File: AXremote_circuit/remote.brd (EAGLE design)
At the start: 60 x 49 mm, 27 parts, among them Q1 16MHz, U1 AX8052F143HS

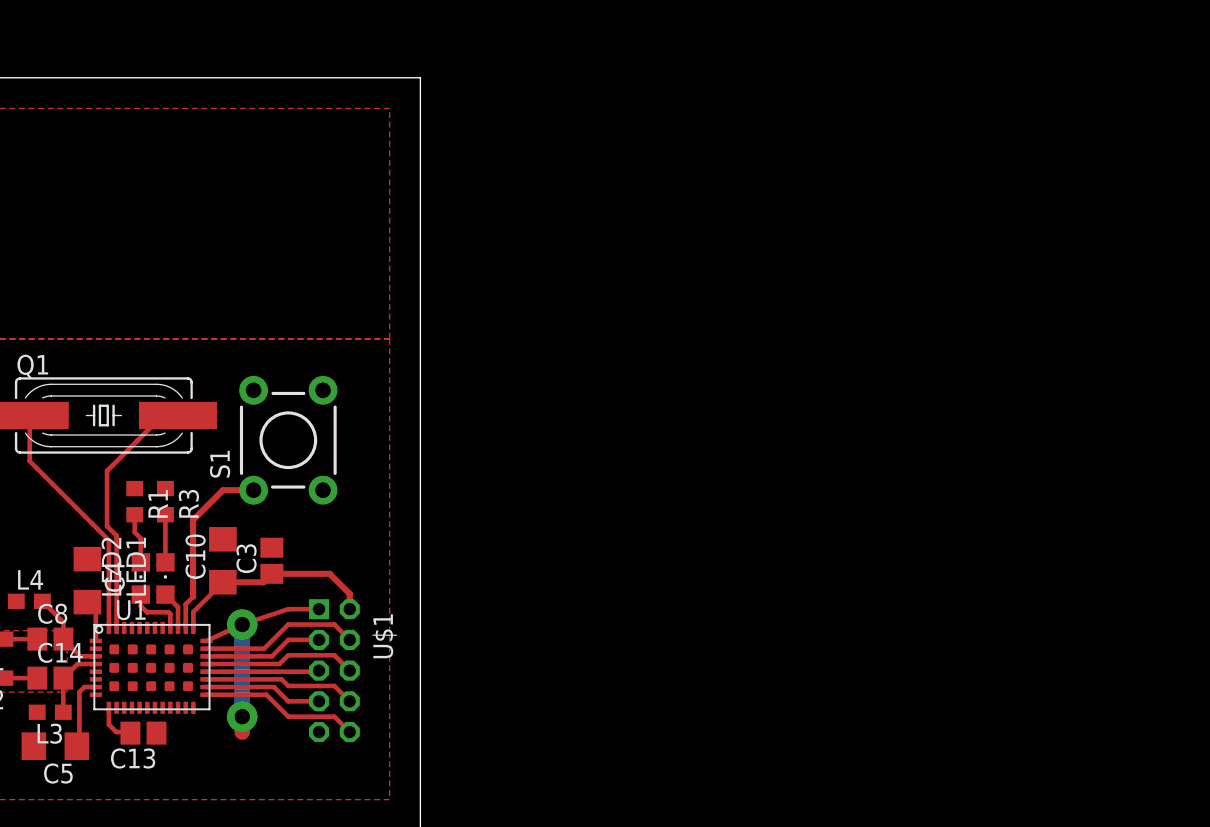
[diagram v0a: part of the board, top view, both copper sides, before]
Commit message: Fix progconnector in schematic. Add TODOs.
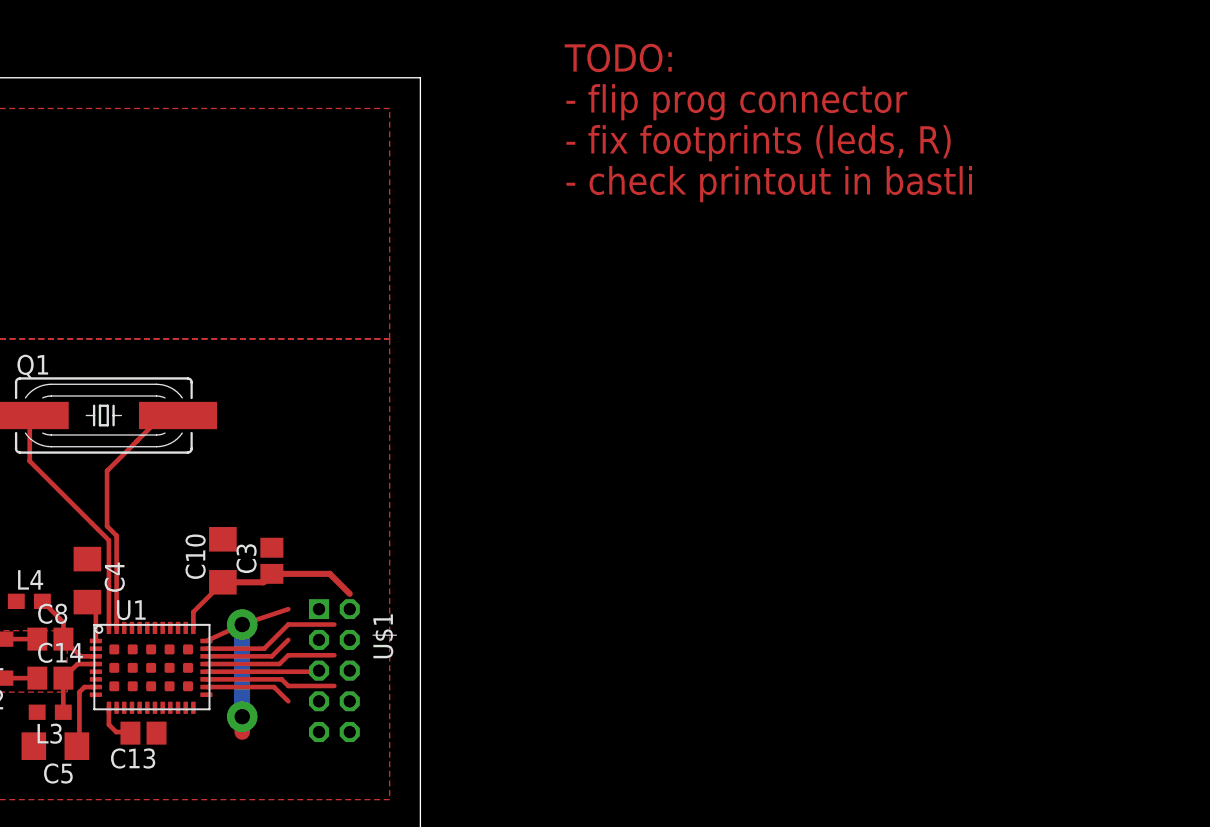
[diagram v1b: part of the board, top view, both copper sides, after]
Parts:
- removed LED1, LED2: (no value), led:CHIPLED_0805
- removed R1, R3: 220, resistor:R0603
- removed S1: SWITCH-MOMENTARY-2PTH, SparkFun-Electromechanical:TACTILE-PTH
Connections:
- removed net N$11: LED1.A, U1.31
- removed net N$18: U$1.P$10, U1.21
- removed net N$19: S1.1, U1.30
- removed net N$4: LED2.C, R1.2
- removed net RST_N: U$1.P$4, U1.27
- new net BATTMEASURE: U1.30
- net DBG_CLK: now also U$1.P$5; no longer U$1.P$6
- net DBG_DATA: now also U$1.P$6; no longer U$1.P$5
- net DBG_EN: now also U$1.P$4; no longer U$1.P$3
- net GND: now also U$1.P$10, U$1.P$2; no longer R1.1, R3.1, S1.3, U$1.P$1, U$1.P$9
- net N$16: now also U$1.P$9, U1.21; no longer LED2.A, U1.32
- net N$5: now also U$1.P$3, U1.27; no longer LED1.C, R3.2
- net RX0: now also U$1.P$7; no longer U$1.P$8
- net TX0: now also U$1.P$8; no longer U$1.P$7
- net VCC: now also U$1.P$1, U1.36; no longer U$1.P$2
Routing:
- net N$19: track 12.0 -> 0.00 mm
- net RST_N: track 10.4 -> 0.00 mm
- net N$18: track 10.3 -> 0.00 mm
- net N$5: track 3.10 -> 8.98 mm
- net N$16: track 3.79 -> 0.00 mm
- net N$4: track 3.27 -> 0.00 mm
- net N$11: track 2.51 -> 0.00 mm
- net TX0: track 7.72 -> 5.72 mm
- net GND: track 41.5 -> 39.5 mm
- net DBG_EN: track 7.77 -> 5.77 mm
- net RX0: track 9.92 -> 8.51 mm
- net DBG_CLK: track 9.98 -> 8.57 mm
- net VCC: track 13.8 -> 12.8 mm
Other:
- board text added: "TODO: - flip prog connector - fix footprints (leds, R) - check printout in bastli"

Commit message: remote almost complete
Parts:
- added C1: 100uF, resistor:PANASONIC_E
- added C2: 100uF, resistor:C1206K
- added JP1: (no value), pinhead:1X02
- added LED1, LED2: (no value), led:CHIPLED_1206
- added R1, R3: (no value), resistor:R0603
- added S1, S10, S11, S12, S13, S14, S15, S16, S17, S18, S19, S2, S20, S21, S22, S23, S24, S25, S28, S3, S30, S4, S41, S42, S43, S44, S45, S46, S5, S6, S7, S8, S9: (no value), switch-omron:B3F-10XX
- added U$2: 2X5PIN-CONNECTOR, sam_eagle_parts:2X5PIN-CONNECTOR-SMD
- C10, C4, C5: device resistor:C1206 -> resistor:C0603
- U$1: value PINHEADER5X2 -> CR2032; device sam:PINHEADER5X2AT2MM -> sam_eagle_parts:CRC2032HOLDER
- moved Q1 39.8 mm to (33.4, 23.0)
- moved U$1 39.5 mm to (58.0, 4.00), turned to 90 degrees
- moved C13 36.4 mm to (39.9, 4.43), turned to 90 degrees
- moved C10 35.8 mm to (46.5, 15.9), turned to 0 degrees
- moved C3 34.2 mm to (46.5, 18.7), turned to 0 degrees
- moved C16 34.0 mm to (30.8, 6.10)
- moved C6 34.0 mm to (23.2, 14.5)
- moved C7 34.0 mm to (23.2, 7.87)
- moved L3 34.0 mm to (35.9, 7.69)
- moved L6 34.0 mm to (28.3, 6.10)
- moved R2 34.0 mm to (24.2, 11.2)
- moved U1 34.0 mm to (42.5, 10.6)
- moved C14 34.0 mm to (35.9, 9.91)
- moved C15 34.0 mm to (28.3, 9.91)
- moved C17 34.0 mm to (29.6, 16.3)
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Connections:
- removed net BATTMEASURE: U1.30
- removed net RX0: U$1.P$7, U1.23
- removed net TX0: U$1.P$8, U1.22
- new net COL0: S1.1, S1.2, S11.1, S11.2, S16.1, S16.2, S21.1, S21.2, S6.1, S6.2, U1.23
- new net COL1: S12.1, S12.2, S17.1, S17.2, S2.1, S2.2, S22.1, S22.2, S7.1, S7.2, U1.22
- new net COL2: S13.1, S13.2, S18.1, S18.2, S23.1, S23.2, S28.1, S28.2, S3.1, S3.2, S8.1, S8.2, U1.21
- new net COL3: S14.1, S14.2, S19.1, S19.2, S24.1, S24.2, S4.1, S4.2, S9.1, S9.2, U1.20
- new net COL4: S10.1, S10.2, S15.1, S15.2, S20.1, S20.2, S25.1, S25.2, S30.1, S30.2, S5.1, S5.2, U1.19
- new net COL5: S41.1, S41.2, S42.1, S42.2, S43.1, S43.2, S44.1, S44.2, S45.1, S45.2, S46.1, S46.2, U1.18
- new net N$11: LED2.A, U1.35
- new net N$17: LED1.C, R1.2
- new net N$4: LED1.A, U1.34
- new net N$64: C1.+, C2.1, JP1.1, U$1.P$PLUS1, U$1.P$PLUS2
- new net ROW0: S1.3, S1.4, S2.3, S2.4, S3.3, S3.4, S4.3, S4.4, S41.3, S41.4, S5.3, S5.4, U1.17
- new net ROW1: S10.3, S10.4, S42.3, S42.4, S6.3, S6.4, S7.3, S7.4, S8.3, S8.4, S9.3, S9.4, U1.16
- new net ROW2: S11.3, S11.4, S12.3, S12.4, S13.3, S13.4, S14.3, S14.4, S15.3, S15.4, S43.3, S43.4, U1.15
- new net ROW3: S16.3, S16.4, S17.3, S17.4, S18.3, S18.4, S19.3, S19.4, S20.3, S20.4, S44.3, S44.4, U1.14
- new net ROW4: S21.3, S21.4, S22.3, S22.4, S23.3, S23.4, S24.3, S24.4, S25.3, S25.4, S45.3, S45.4, U1.13
- new net ROW5: S28.3, S28.4, S30.3, S30.4, S46.3, S46.4, U1.30
- new net ROW6: U1.31
- new net ROW7: U1.32
- new net ROW8: U1.33
- net DBG_CLK: now also U$2.P$5; no longer U$1.P$5
- net DBG_DATA: now also U$2.P$6; no longer U$1.P$6
- net DBG_EN: now also U$2.P$4; no longer U$1.P$4
- net GND: now also C1.-, C2.2, R1.1, R3.1, U$1.P$MINUS, U$2.P$10, U$2.P$2; no longer U$1.P$10, U$1.P$2
- net N$16: now also LED2.C, R3.2; no longer U$1.P$9, U1.21
- net N$5: now also U$2.P$3; no longer U$1.P$3
- net VCC: now also JP1.2, U$2.P$1; no longer U$1.P$1
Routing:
- net COL4: track 0.00 -> 444.3 mm
- net COL2: track 0.00 -> 405.8 mm
- net ROW5: track 0.00 -> 299.6 mm
- net ROW4: track 0.00 -> 283.1 mm
- net ROW0: track 0.00 -> 259.0 mm
- net ROW3: track 0.00 -> 254.0 mm
- net ROW2: track 0.00 -> 237.1 mm
- net COL5: track 0.00 -> 235.7 mm
- net COL0: track 0.00 -> 228.9 mm
- net COL3: track 0.00 -> 221.8 mm
- net COL1: track 0.00 -> 221.0 mm
- net ROW1: track 0.00 -> 176.6 mm
- net VCC: track 12.8 -> 49.0 mm, vias 0 -> 2
- net DBG_EN: track 5.77 -> 38.2 mm
- net DBG_DATA: track 7.26 -> 35.4 mm
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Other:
- board size 60 x 49 mm -> 247.5 x 49 mm
- board text removed: "TODO: - flip prog connector - fix footprints (leds, R) - check printout in bastli"

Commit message: Remote and receiver done.
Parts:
- added U$3: APERTURE_LOGO, sam_eagle_parts:APERTURE_LOGO
- moved Q1 2.00 mm to (31.4, 23.0)
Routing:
- net GND: track 43.3 -> 137.9 mm, vias 2 -> 6
- net N$64: track 25.7 -> 36.2 mm, vias 1 -> 2
- net N$15: track 18.2 -> 20.2 mm
- net COL2: track 405.8 -> 407.2 mm
- net ROW5: track 299.6 -> 301.0 mm
- net COL4: track 444.3 -> 445.3 mm
- net COL3: track 221.8 -> 222.6 mm
- net N$14: track 10.7 -> 11.4 mm
- net ROW0: track 259.0 -> 259.6 mm
- net VCC: track 49.0 -> 49.6 mm
- net COL5: track 235.7 -> 236.3 mm
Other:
- board size 247.5 x 49 mm -> 240 x 49 mm
- board text added: "Samuel Bryner, 2013, rev 2"
- board text removed: "Samuel Bryner, 2013 AX8052F143 Test rev 1b"

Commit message: Added a few keys.
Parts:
- added R4: (no value), resistor:R0603
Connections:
- removed net N$64: C1.+, C2.1, JP1.1, U$1.P$PLUS1, U$1.P$PLUS2
- new net N$18: C1.+, C2.1, JP1.1, R4.2, U$1.P$PLUS1, U$1.P$PLUS2
- net N$5: now also R4.1
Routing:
- net N$18: track 0.00 -> 37.7 mm, vias 0 -> 2
- net N$64: track 36.2 -> 0.00 mm, vias 2 -> 0
- net COL0: track 228.9 -> 235.4 mm
- net GND: track 137.9 -> 139.6 mm
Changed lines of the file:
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@@
 <hole x="87" y="19" drill="3"/>
 <hole x="197" y="45" drill="3"/>
+<hole x="127.5" y="7" drill="3"/>
 </plain>
 <attributes>
@@
 </element>
 <element name="U$3" library="sam_eagle_parts" package="APERTURE_LOGO" value="APERTURE_LOGO" x="178" y="19"/>
+<element name="R4" library="resistor" package="R0603" value="" x="53" y="19" rot="R90"/>
 </elements>
 <signals>
@@
 <wire x1="34" y1="18" x2="33.11" y2="17.11" width="0.4064" layer="1"/>
 <wire x1="33.11" y1="17.11" x2="29.56" y2="17.11" width="0.4064" layer="1"/>
-<wire x1="38.87" y1="9.83" x2="38.87" y2="8.83" width="0" layer="19" extent="1-1"/>
+<wire x1="38.87" y1="9.83" x2="40.07" y2="9.83" width="0.3" layer="1"/>
+<wire x1="40.07" y1="9.83" x2="40.07" y2="9.38" width="0.3" layer="1"/>
 </signal>
 <signal name="N$1">
@@
 <wire x1="53" y1="18" x2="58" y2="18" width="0.3048" layer="1"/>
 <wire x1="58" y1="18" x2="61" y2="21" width="0.3048" layer="1"/>
+<contactref element="R4" pad="1"/>
+<wire x1="53" y1="18.15" x2="53" y2="18" width="0.4064" layer="1"/>
 </signal>
 <signal name="ROW0">
@@
 <wire x1="85.5" y1="41" x2="73" y2="41" width="0.4064" layer="1"/>
 <wire x1="73" y1="41" x2="70" y2="38" width="0.4064" layer="1"/>
-<wire x1="184.4988" y1="39.2606" x2="191.0012" y2="39.2606" width="0" layer="19" extent="1-1"/>
+<wire x1="184.4988" y1="39.2606" x2="191.0012" y2="39.2606" width="0.4064" layer="16"/>
 </signal>
 <signal name="ROW1">
@@
 <signal name="ROW7">
 <contactref element="U1" pad="32"/>
-</signal>
-<signal name="N$64">
-<contactref element="C2" pad="1"/>
-<contactref element="C1" pad="+"/>
-<contactref element="JP1" pad="1"/>
-<contactref element="U$1" pad="P$PLUS2"/>
-<contactref element="U$1" pad="P$PLUS1"/>
-<wire x1="56" y1="21" x2="52.5" y2="21" width="0.4064" layer="1"/>
-<wire x1="52.5" y1="21" x2="51" y2="22.5" width="0.4064" layer="1"/>
-<via x="51" y="19" extent="1-16" drill="0.9" diameter="1.4224" shape="square"/>
-<wire x1="51" y1="19" x2="51" y2="22.5" width="0.4064" layer="1"/>
-<wire x1="58.5" y1="29.73" x2="58.5" y2="23.5" width="0.4064" layer="1"/>
-<wire x1="58.5" y1="23.5" x2="56" y2="21" width="0.4064" layer="1"/>
-<wire x1="52.92" y1="9.08" x2="52.92" y2="10.479771875" width="0.4064" layer="1"/>
-<wire x1="52.92" y1="10.479771875" x2="52.92" y2="11.62" width="0.4064" layer="1"/>
-<wire x1="52.92" y1="10.479771875" x2="50.979771875" y2="10.479771875" width="0.4064" layer="1"/>
-<wire x1="50.979771875" y1="10.479771875" x2="50.5" y2="10" width="0.4064" layer="1"/>
-<via x="50.5" y="10" extent="1-16" drill="0.9" diameter="1.4224" shape="square"/>
-<wire x1="50.5" y1="10" x2="50.5" y2="18.5" width="0.4064" layer="16"/>
-<wire x1="50.5" y1="18.5" x2="51" y2="19" width="0.4064" layer="16"/>
-<wire x1="50.5" y1="10" x2="51.5" y2="9" width="0.4064" layer="1"/>
-<wire x1="51.5" y1="9" x2="53" y2="9" width="0.4064" layer="1"/>
 </signal>
 <signal name="COL1">
@@
 <wire x1="56" y1="39" x2="56" y2="41" width="0.4064" layer="1"/>
 <wire x1="56" y1="41" x2="58" y2="43" width="0.4064" layer="1"/>
-<wire x1="147" y1="43" x2="192.5" y2="43" width="0.4064" layer="1"/>
-<wire x1="192.5" y1="43" x2="194.5" y2="41" width="0.4064" layer="1"/>
-<wire x1="194.5" y1="41" x2="199.5" y2="41" width="0.4064" layer="1"/>
-<wire x1="199.5" y1="41" x2="201.5" y2="43" width="0.4064" layer="1"/>
-<wire x1="201.5" y1="43" x2="211.5" y2="43" width="0.4064" layer="1"/>
+<wire x1="147" y1="43" x2="192" y2="43" width="0.4064" layer="1"/>
+<wire x1="192" y1="43" x2="194" y2="41" width="0.4064" layer="1"/>
+<wire x1="194" y1="41" x2="200" y2="41" width="0.4064" layer="1"/>
+<wire x1="200" y1="41" x2="202" y2="43" width="0.4064" layer="1"/>
+<wire x1="202" y1="43" x2="211.5" y2="43" width="0.4064" layer="1"/>
 </signal>
 <signal name="COL3">
@@
 <wire x1="136" y1="14" x2="122.5118" y2="14" width="0.4064" layer="1"/>
 <wire x1="122.5118" y1="14" x2="122.2512" y2="14.2606" width="0.4064" layer="1"/>
-<wire x1="212" y1="44" x2="201" y2="44" width="0.4064" layer="1"/>
-<wire x1="201" y1="44" x2="199" y2="42" width="0.4064" layer="1"/>
-<wire x1="199" y1="42" x2="195" y2="42" width="0.4064" layer="1"/>
-<wire x1="195" y1="42" x2="193" y2="44" width="0.4064" layer="1"/>
-<wire x1="193" y1="44" x2="147.5" y2="44" width="0.4064" layer="1"/>
+<wire x1="212" y1="44" x2="201.5" y2="44" width="0.4064" layer="1"/>
+<wire x1="201.5" y1="44" x2="199.5" y2="42" width="0.4064" layer="1"/>
+<wire x1="199.5" y1="42" x2="194.5" y2="42" width="0.4064" layer="1"/>
+<wire x1="194.5" y1="42" x2="192.5" y2="44" width="0.4064" layer="1"/>
+<wire x1="192.5" y1="44" x2="147.5" y2="44" width="0.4064" layer="1"/>
 </signal>
 <signal name="N$4">
@@
 <contactref element="R3" pad="2"/>
 <contactref element="LED2" pad="C"/>
-<wire x1="29.75" y1="30" x2="28" y2="30" width="0.3048" layer="1"/>
-<wire x1="27.85" y1="30" x2="28" y2="30" width="0" layer="19" extent="1-1"/>
+<wire x1="27.85" y1="30" x2="29.75" y2="30" width="0.4064" layer="1"/>
 </signal>
 <signal name="N$17">
@@
 <wire x1="134.4988" y1="12.2606" x2="134.4988" y2="11.5012" width="0.4064" layer="1"/>
 </signal>
+<signal name="N$18">
+<contactref element="R4" pad="2"/>
+<contactref element="C2" pad="1"/>
+<contactref element="C1" pad="+"/>
+<contactref element="JP1" pad="1"/>
+<contactref element="U$1" pad="P$PLUS2"/>
+<contactref element="U$1" pad="P$PLUS1"/>
+<wire x1="56" y1="21" x2="53" y2="21" width="0.4064" layer="1"/>
+<wire x1="53" y1="21" x2="52.5" y2="21" width="0.4064" layer="1"/>
+<wire x1="52.5" y1="21" x2="51" y2="22.5" width="0.4064" layer="1"/>
+<via x="50" y="18" extent="1-16" drill="0.9" diameter="1.4224" shape="square"/>
+<wire x1="58.5" y1="29.73" x2="58.5" y2="23.5" width="0.4064" layer="1"/>
+<wire x1="58.5" y1="23.5" x2="56" y2="21" width="0.4064" layer="1"/>
+<wire x1="52.92" y1="9.08" x2="52.92" y2="10.479771875" width="0.4064" layer="1"/>
+<wire x1="52.92" y1="10.479771875" x2="52.92" y2="11.62" width="0.4064" layer="1"/>
+<wire x1="52.92" y1="10.479771875" x2="50.979771875" y2="10.479771875" width="0.4064" layer="1"/>
+<wire x1="50.979771875" y1="10.479771875" x2="50.5" y2="10" width="0.4064" layer="1"/>
+<via x="50.5" y="10" extent="1-16" drill="0.9" diameter="1.4224" shape="square"/>
+<wire x1="50.5" y1="10" x2="50.5" y2="17.5" width="0.4064" layer="16"/>
+<wire x1="50.5" y1="17.5" x2="50" y2="18" width="0.4064" layer="16"/>
+<wire x1="50.5" y1="10" x2="51.5" y2="9" width="0.4064" layer="1"/>
+<wire x1="51.5" y1="9" x2="53" y2="9" width="0.4064" layer="1"/>
+<wire x1="53" y1="19.85" x2="53" y2="21" width="0.4064" layer="1"/>
+<wire x1="51" y1="22.5" x2="51" y2="19" width="0.4064" layer="1"/>
+<wire x1="51" y1="19" x2="50" y2="18" width="0.4064" layer="1"/>
+</signal>
 </signals>

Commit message: Start rev 3, full SMD.
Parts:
- removed JP1: (no value), pinhead:1X02
- removed S41, S42, S43, S44, S45, S46: (no value), switch-omron:B3F-10XX
- added S26, S27, S29, S31, S32, S34: SWITCHSMD, sam:TACTILE_SWITCH_FSM2JSMA
- S1, S10, S11, S12, S13, S14, S15, S16, S17, S18, S19, S2, S20, S21, S22, S23, S24, S25, S28, S3, S30, S4, S5, S6, S7, S8, S9: value (none) -> SWITCHSMD; device switch-omron:B3F-10XX -> sam:TACTILE_SWITCH_FSM2JSMA
- moved S28 301.7 mm to (-58.0, -95.0)
- moved S22 285.7 mm to (-58.0, -71.0)
- moved S30 283.9 mm to (-44.0, -95.0)
- moved S24 268.1 mm to (-44.0, -71.0)
- moved S25 263.5 mm to (-58.0, -83.0)
- moved S23 257.1 mm to (-51.0, -71.0)
- moved S21 250.8 mm to (-44.0, -59.0)
- moved S19 241.9 mm to (-58.0, -59.0)
- moved S17 235.5 mm to (-51.0, -47.0)
- moved S16 230.4 mm to (-58.0, -47.0)
- moved S20 219.3 mm to (-51.0, -59.0)
- moved S18 212.9 mm to (-44.0, -47.0)
- moved S14 199.6 mm to (-51.0, -35.0)
- moved S12 192.4 mm to (-44.0, -23.0)
- moved S13 186.7 mm to (-58.0, -35.0)
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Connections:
- removed net N$18: C1.+, C2.1, JP1.1, R4.2, U$1.P$PLUS1, U$1.P$PLUS2
- new net ROW10: S16.P3
- new net ROW11: S22.P3
- new net ROW12: S28.P3
- new net ROW13: S34.P3
- new net ROW9: S10.P3
- net COL0: now also S1.P1, S1.P2; no longer S1.1, S1.2, S11.1, S11.2, S16.1, S16.2, S21.1, S21.2, S6.1, S6.2
- net COL1: now also S2.P1, S2.P2; no longer S12.1, S12.2, S17.1, S17.2, S2.1, S2.2, S22.1, S22.2, S7.1, S7.2
- net COL2: now also S3.P1, S3.P2; no longer S13.1, S13.2, S18.1, S18.2, S23.1, S23.2, S28.1, S28.2, S3.1, S3.2, S8.1, S8.2
- net COL3: now also S4.P1, S4.P2; no longer S14.1, S14.2, S19.1, S19.2, S24.1, S24.2, S4.1, S4.2, S9.1, S9.2
- net COL4: now also S5.P1, S5.P2; no longer S10.1, S10.2, S15.1, S15.2, S20.1, S20.2, S25.1, S25.2, S30.1, S30.2, S5.1, S5.2
- net COL5: now also S6.P1, S6.P2; no longer S41.1, S41.2, S42.1, S42.2, S43.1, S43.2, S44.1, S44.2, S45.1, S45.2, S46.1, S46.2
- net ROW0: now also S1.P3, S1.P4, S2.P3, S2.P4, S3.P3, S3.P4, S4.P3, S4.P4, S5.P3, S5.P4, S6.P3, S6.P4; no longer S1.3, S1.4, S2.3, S2.4, S3.3, S3.4, S4.3, S4.4, S41.3, S41.4, S5.3, S5.4
- net ROW1: no longer S10.3, S10.4, S42.3, S42.4, S6.3, S6.4, S7.3, S7.4, S8.3, S8.4, S9.3, S9.4
- net ROW2: no longer S11.3, S11.4, S12.3, S12.4, S13.3, S13.4, S14.3, S14.4, S15.3, S15.4, S43.3, S43.4
- net ROW3: no longer S16.3, S16.4, S17.3, S17.4, S18.3, S18.4, S19.3, S19.4, S20.3, S20.4, S44.3, S44.4
- net ROW4: no longer S21.3, S21.4, S22.3, S22.4, S23.3, S23.4, S24.3, S24.4, S25.3, S25.4, S45.3, S45.4
- net ROW5: no longer S28.3, S28.4, S30.3, S30.4, S46.3, S46.4
- net VCC: now also C1.+, C2.1, R4.2, U$1.P$PLUS1, U$1.P$PLUS2; no longer JP1.2
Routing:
- net COL4: track 445.3 -> 0.00 mm
- net COL2: track 407.2 -> 0.00 mm
- net ROW5: track 301.0 -> 0.00 mm
- net ROW4: track 282.8 -> 0.00 mm
- net ROW0: track 259.6 -> 0.00 mm
- net ROW3: track 254.0 -> 0.00 mm
- net ROW2: track 237.1 -> 0.00 mm
- net COL5: track 236.3 -> 0.00 mm
- net COL0: track 235.4 -> 0.00 mm
- net COL3: track 222.6 -> 0.00 mm
- net COL1: track 221.0 -> 0.00 mm
- net ROW1: track 176.6 -> 0.00 mm
- net GND: track 139.6 -> 50.7 mm, vias 6 -> 3
- net N$18: track 37.7 -> 0.00 mm, vias 2 -> 0
- net VCC: track 49.6 -> 76.1 mm, vias 2 -> 4
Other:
- board text added: "Samuel Bryner, 2014, rev 3"
- board text removed: "Samuel Bryner, 2013, rev 2"
